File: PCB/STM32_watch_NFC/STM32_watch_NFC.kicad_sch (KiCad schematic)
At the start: 45 parts, among them J1 Conn_01x05_Pin, Q1 2N7000, SW1 SW_DPST_x2, SW1 SW_MEC_5G, SW2 SW_MEC_5G, U1 STM32L031G6Ux, Y2 32.768kHz

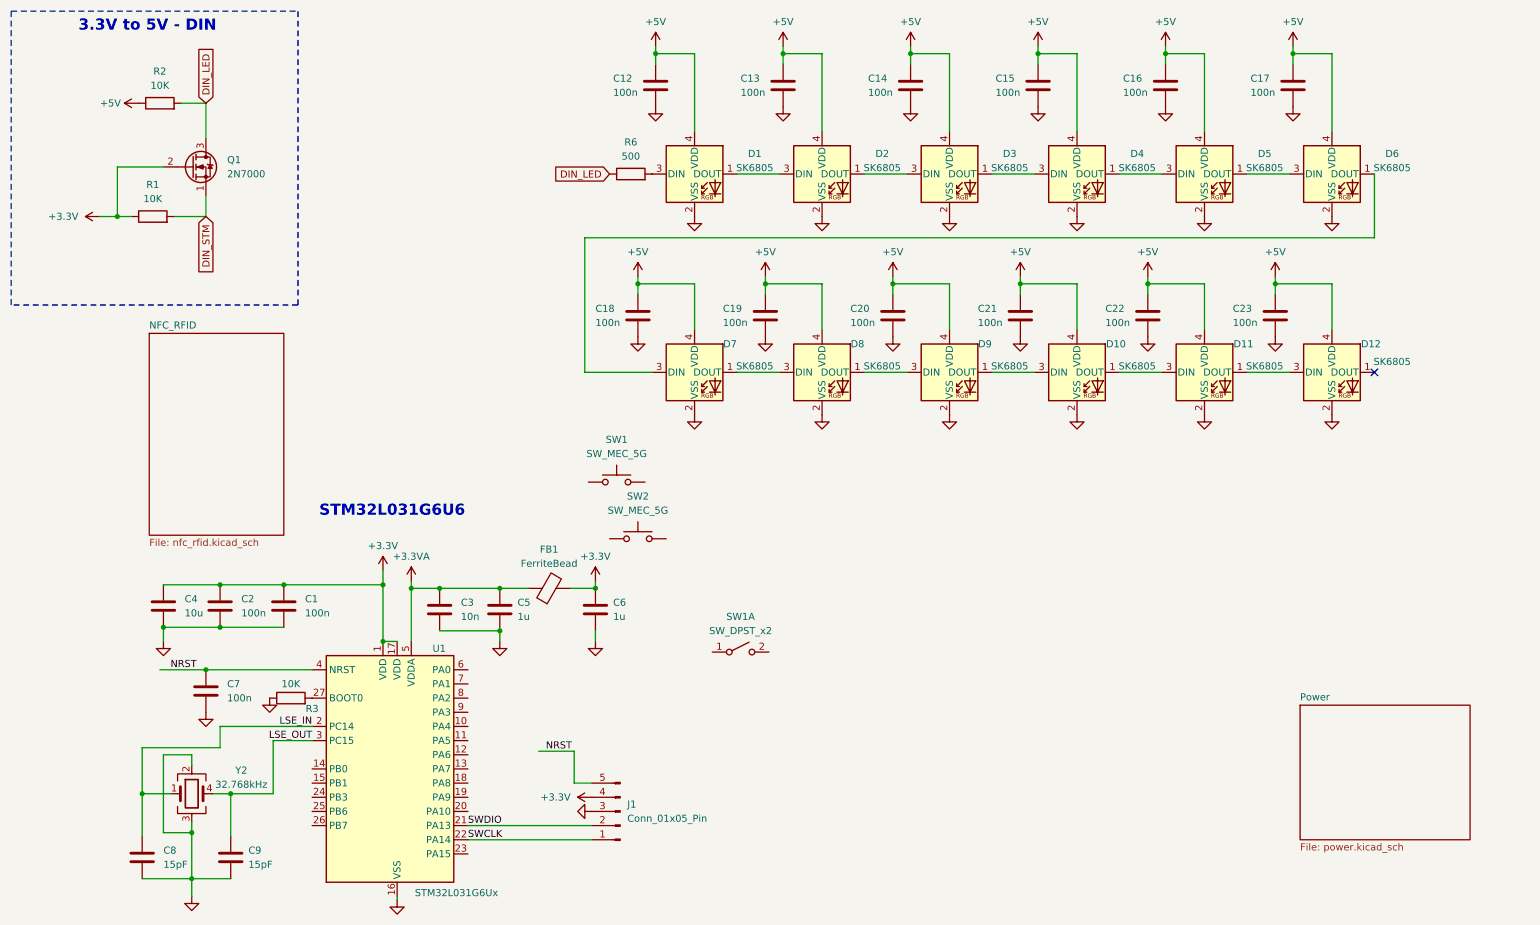
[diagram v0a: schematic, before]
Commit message: Kicad
Everything about power, started to make nfc - spiral antenna problem
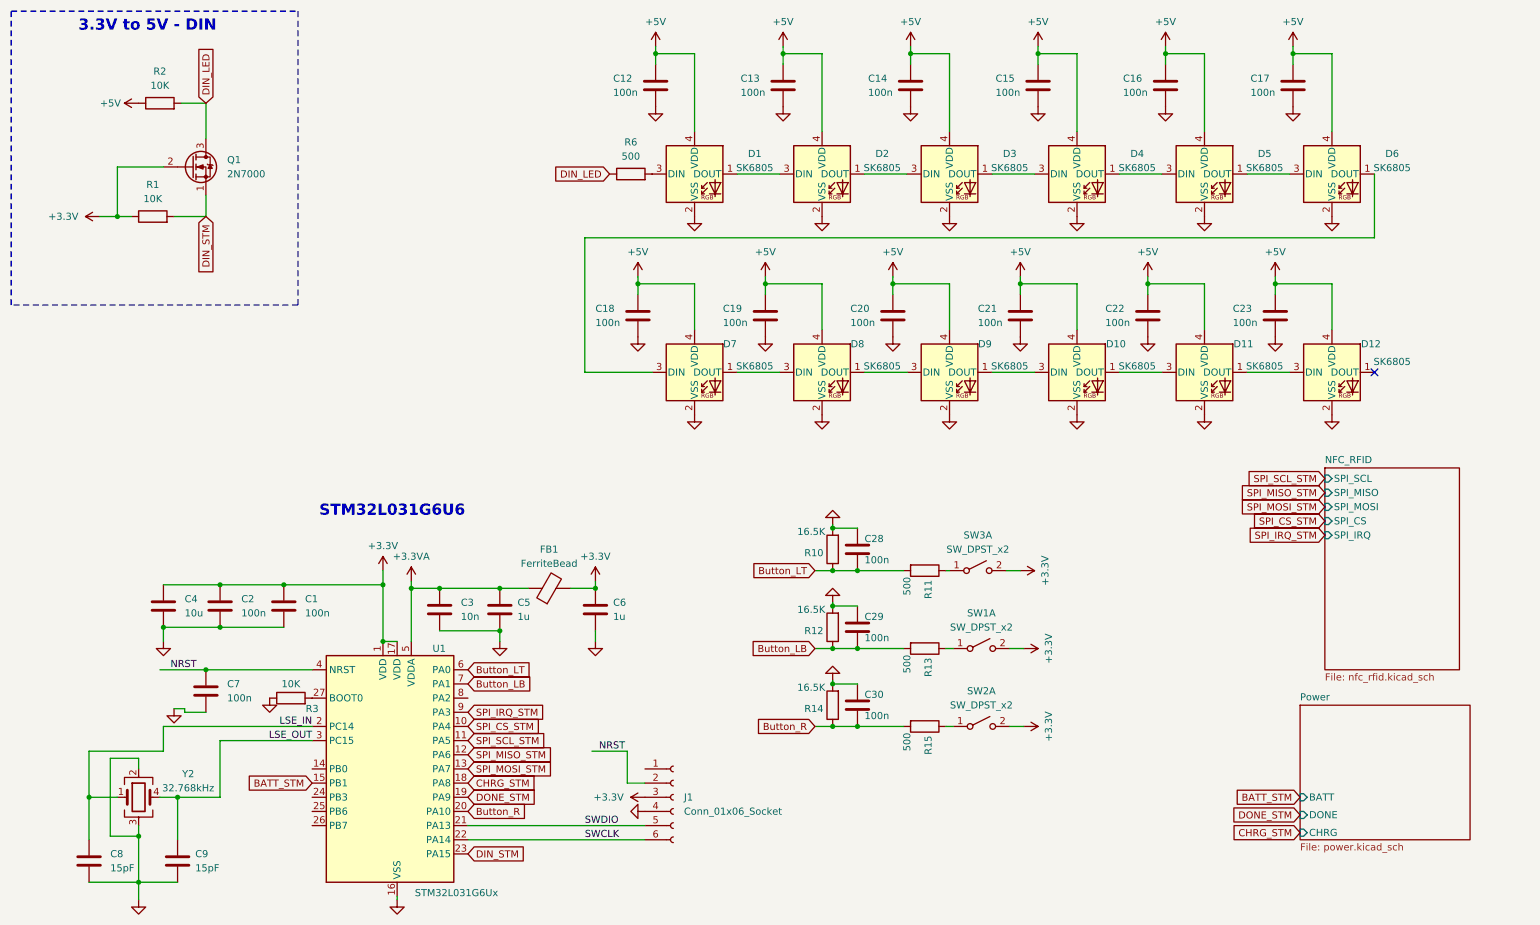
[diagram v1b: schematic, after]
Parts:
- removed J1: Conn_01x05_Pin, symbol Connector:Conn_01x05_Pin
- removed SW1, SW2: SW_MEC_5G, symbol Switch:SW_MEC_5G
- added C28, C29, C30: 100n, Capacitor_SMD:C_0402_1005Metric, symbol Device:C
- added J1: Conn_01x06_Socket, Connector_JST:JST_SUR_SM05B-SURS-TF_1x05-1MP_P0.80mm_Horizontal, symbol Connector:Conn_01x06_Socket
- added R10, R12, R14: 16.5K, Resistor_SMD:R_0402_1005Metric, symbol Device:R
- added R11, R13, R15: 500, Resistor_SMD:R_0402_1005Metric, symbol Device:R
- added SW2, SW3: SW_DPST_x2, Button_Switch_SMD:Panasonic_EVQPUJ_EVQPUA, symbol Switch:SW_DPST_x2
- R6: footprint (none) -> Resistor_SMD:R_0402_1005Metric
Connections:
- net +3.3V: now also SW1.2 (B), J1.3 (Pin_3), SW2.2 (B), SW3.2 (B)
- net DIN_STM: now also U1.23 (PA15)
- net GND: now also C28.1, C29.1, C30.1, J1.4 (Pin_4), R10.2, R12.2, R14.2
- net NRST: now also J1.2 (Pin_2)
- net SWCLK: now also J1.6 (Pin_6)
- net SWDIO: now also J1.5 (Pin_5)
- net SPI_CS_STM: now reaches U1.10 (PA4)
- net SPI_SCL_STM: now reaches U1.11 (PA5)
- net SPI_MISO_STM: now reaches U1.12 (PA6)
- net SPI_MOSI_STM: now reaches U1.13 (PA7)
- net BATT_STM: now reaches U1.15 (PB1)
- net CHRG_STM: now reaches U1.18 (PA8)
- net DONE_STM: now reaches U1.19 (PA9)
- net Button_R: now reaches U1.20 (PA10)
- net Button_R: now also C30.2, R14.1, R15.2
- net Button_LT: now reaches U1.6 (PA0)
- net Button_LT: now also C28.2, R10.1, R11.2
- net Button_LB: now reaches U1.7 (PA1)
- net Button_LB: now also C29.2, R12.1, R13.2
- net SPI_IRQ_STM: now reaches U1.9 (PA3)
- net at SW1.1 (A): now also R13.1
- new net: R15.1, SW2.1 (A)
- new net: R11.1, SW3.1 (A)
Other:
- sheet NFC_RFID ports: added SPI_CS, SPI_IRQ, SPI_MISO, SPI_MOSI, SPI_SCL; removed none
- sheet Power ports: added BATT, CHRG, DONE; removed none
- moved on the sheet: C8, C9, SW1A, Y2

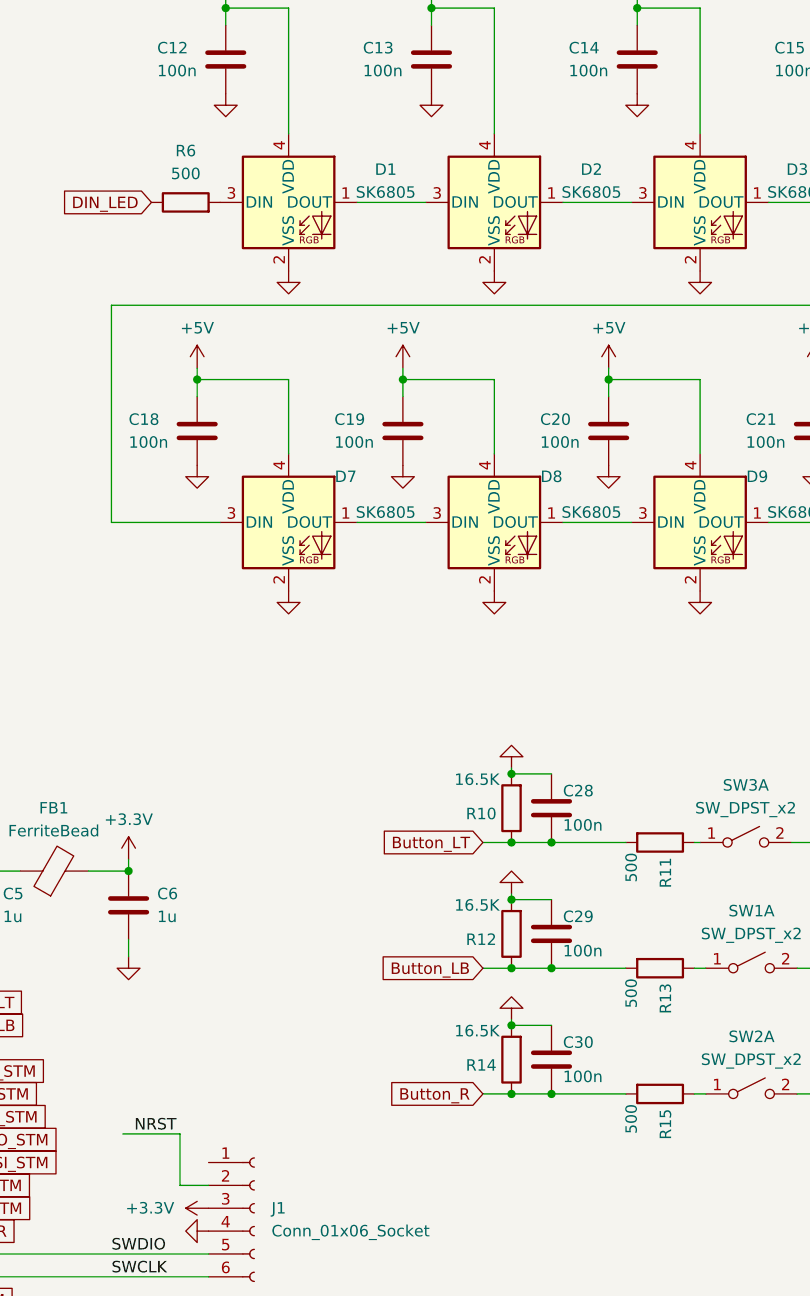
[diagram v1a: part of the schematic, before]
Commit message: Kicad - LCSC, footprints
I managed to add all (I hope so :) ) LCSC values - which component will be used. With that I could determine all footprints
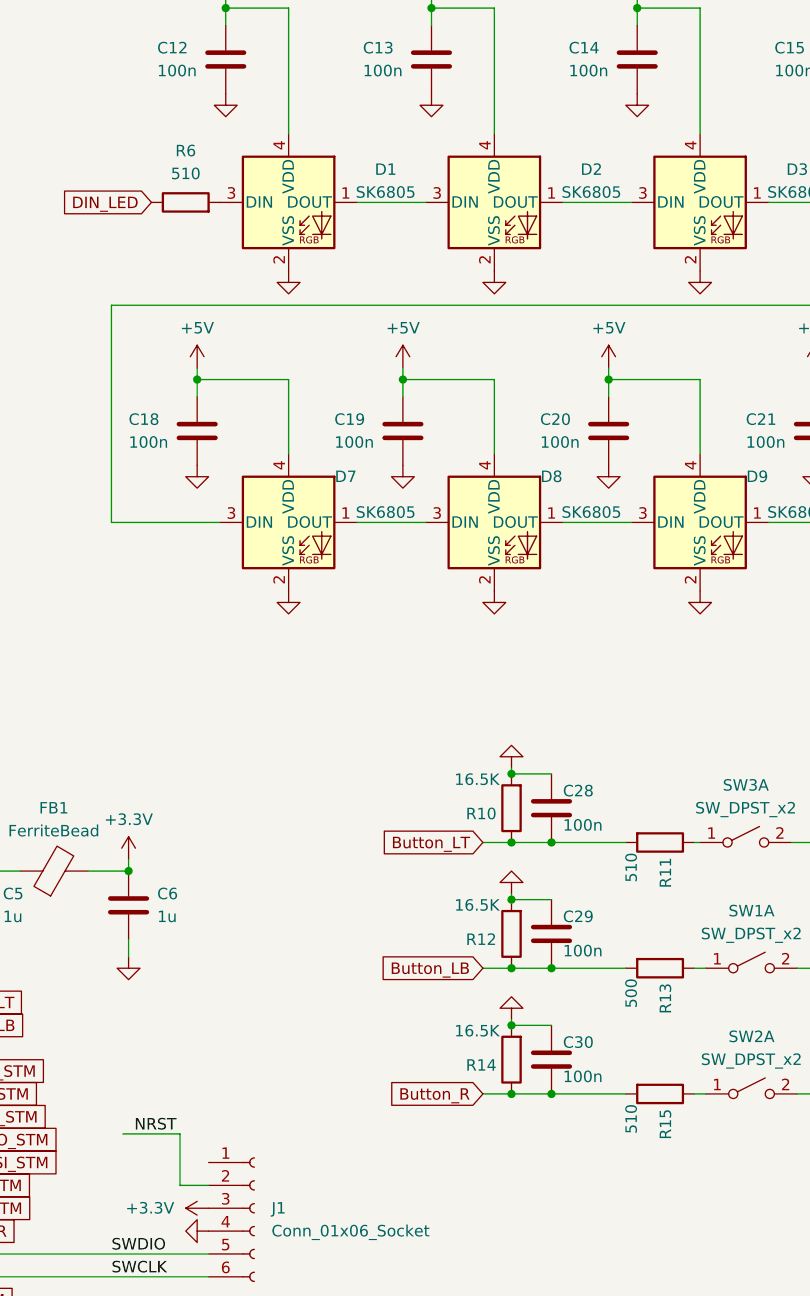
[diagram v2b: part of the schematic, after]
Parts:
- C1, C12, C13, C14, C15, C16, C17, C18, C19, C2, C20, C21, C22, C23, C28, C29, C30, C7: footprint Capacitor_SMD:C_0402_1005Metric -> Capacitor_SMD:C_0201_0603Metric; LCSC (none) -> C7393837
- C3: footprint Capacitor_SMD:C_0402_1005Metric -> Capacitor_SMD:C_0201_0603Metric; LCSC (none) -> C541216
- C4: LCSC (none) -> C77040
- C5, C6: LCSC (none) -> C412453
- C8, C9: LCSC (none) -> C327787
- D1, D10, D11, D12, D2, D3, D4, D5, D6, D7, D8, D9: LCSC (none) -> C2890035
- FB1: LCSC (none) -> C1002
- Q1: LCSC (none) -> C414015
- R1, R2, R3: LCSC (none) -> C308028
- R10: LCSC (none) -> C104028
- R11, R15, R6: value 500 -> 510; LCSC (none) -> C103085
- R12, R14: footprint Resistor_SMD:R_0402_1005Metric -> Resistor_SMD:R_0805_2012Metric; LCSC (none) -> C104028
- R13: LCSC (none) -> C103085
- SW1, SW2, SW3: LCSC (none) -> C128539
- U1: LCSC (none) -> C96514
- Y2: footprint (none) -> Crystal:Crystal_SMD_SeikoEpson_MC146-4Pin_6.7x1.5mm; LCSC (none) -> C7466130
